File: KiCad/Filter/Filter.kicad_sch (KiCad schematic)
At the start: 31 parts, among them J1 Screw_Terminal_01x03, J2 Screw_Terminal_01x03, U1 TL074, U2 TL074

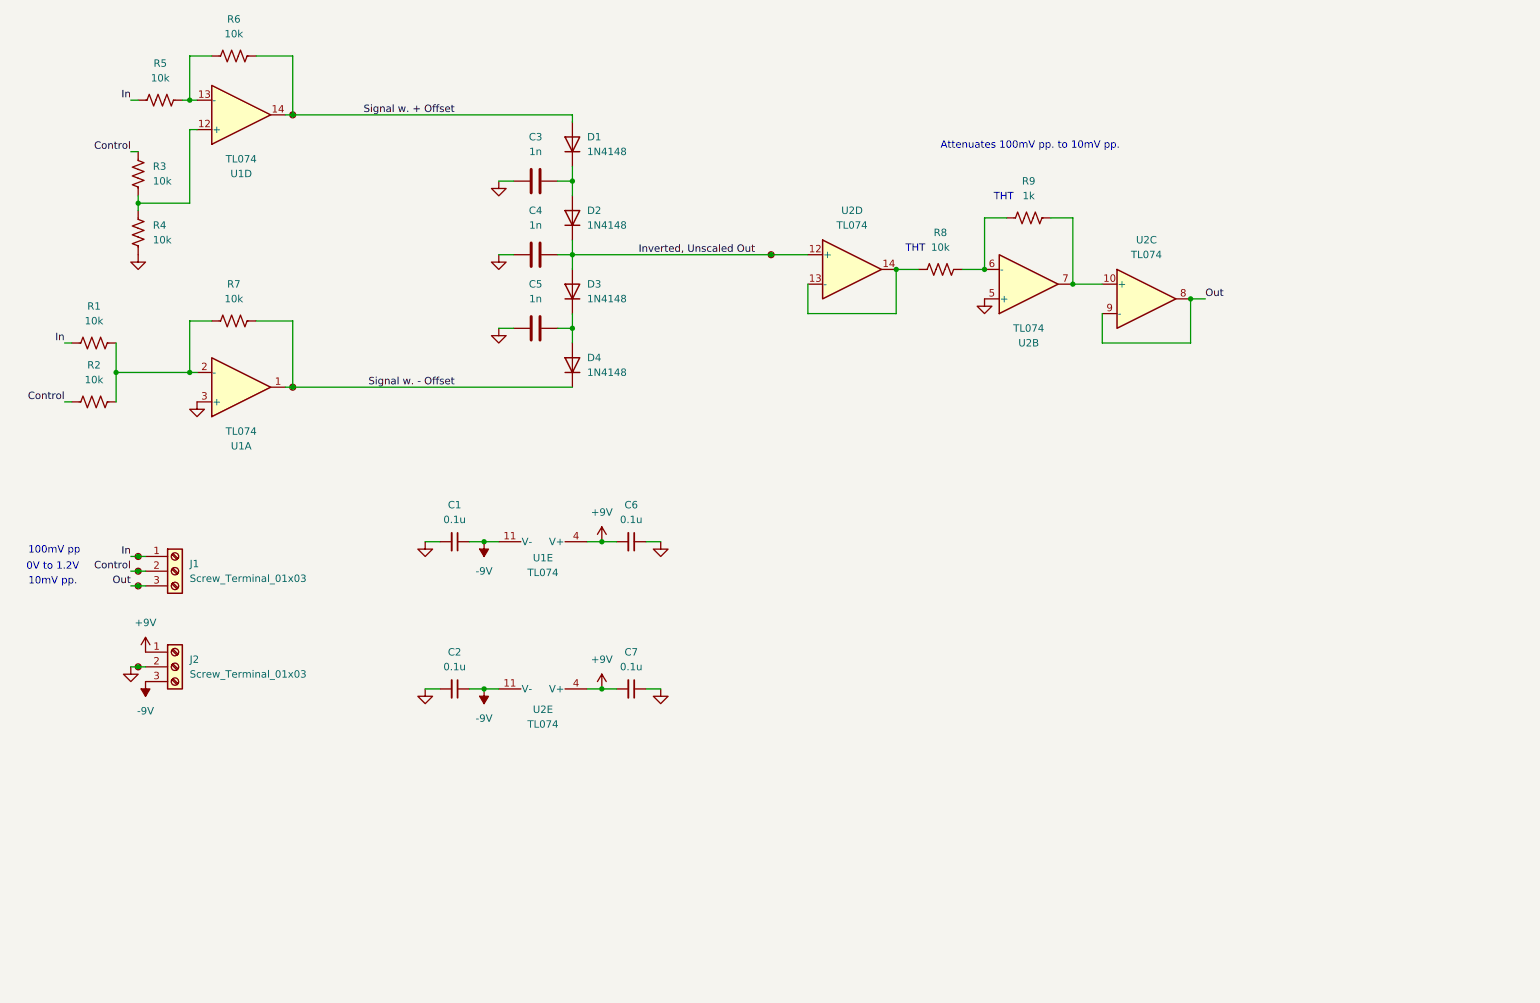
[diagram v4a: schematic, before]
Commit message: added power indicator LEDs
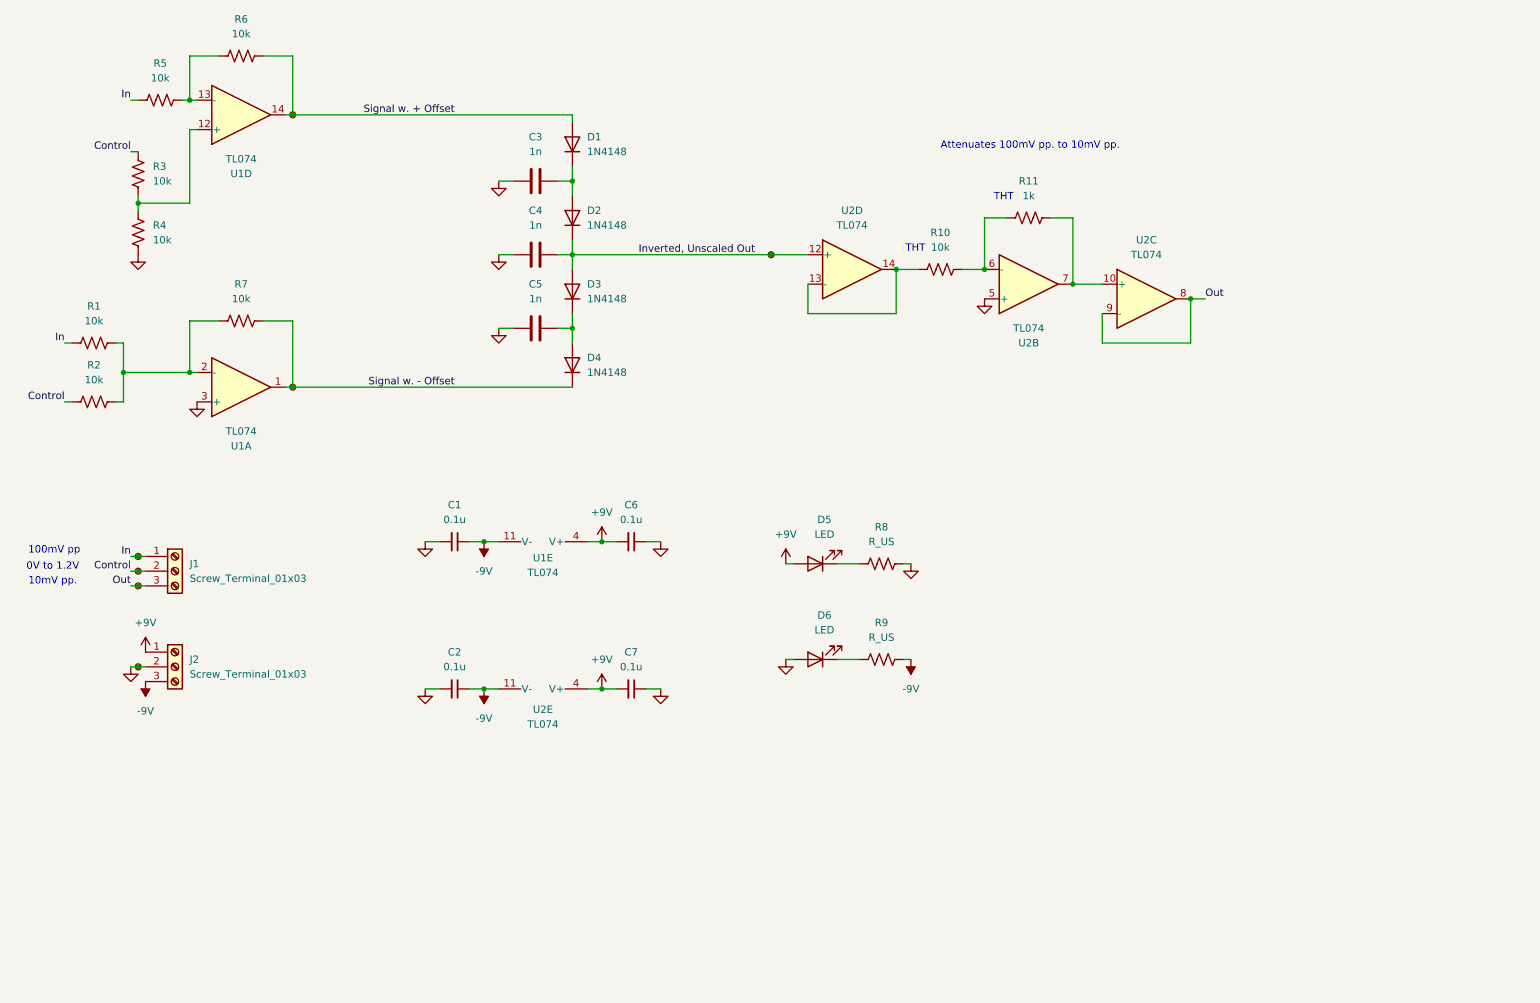
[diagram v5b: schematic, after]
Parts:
- added D5, D6: LED, symbol Device:LED
- added R8, R9: R_US, symbol Device:R_US
- gave numbers to parts that had none: 7
- renumbered R8 to R10, R9 to R11
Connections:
- net +9V: now also D5.2 (A)
- net -9V: now also R9.2
- net GND: now also D6.2 (A), R8.2
- new net: D5.1 (K), R8.1
- new net: D6.1 (K), R9.1
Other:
- moved on the sheet: R6, R7

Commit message: removed unnecessary buffer before filter's output
this drops the number of op amps from 5 to 4, allowing us to use 1 IC instead of 2 ICs with 3 unused circuits.
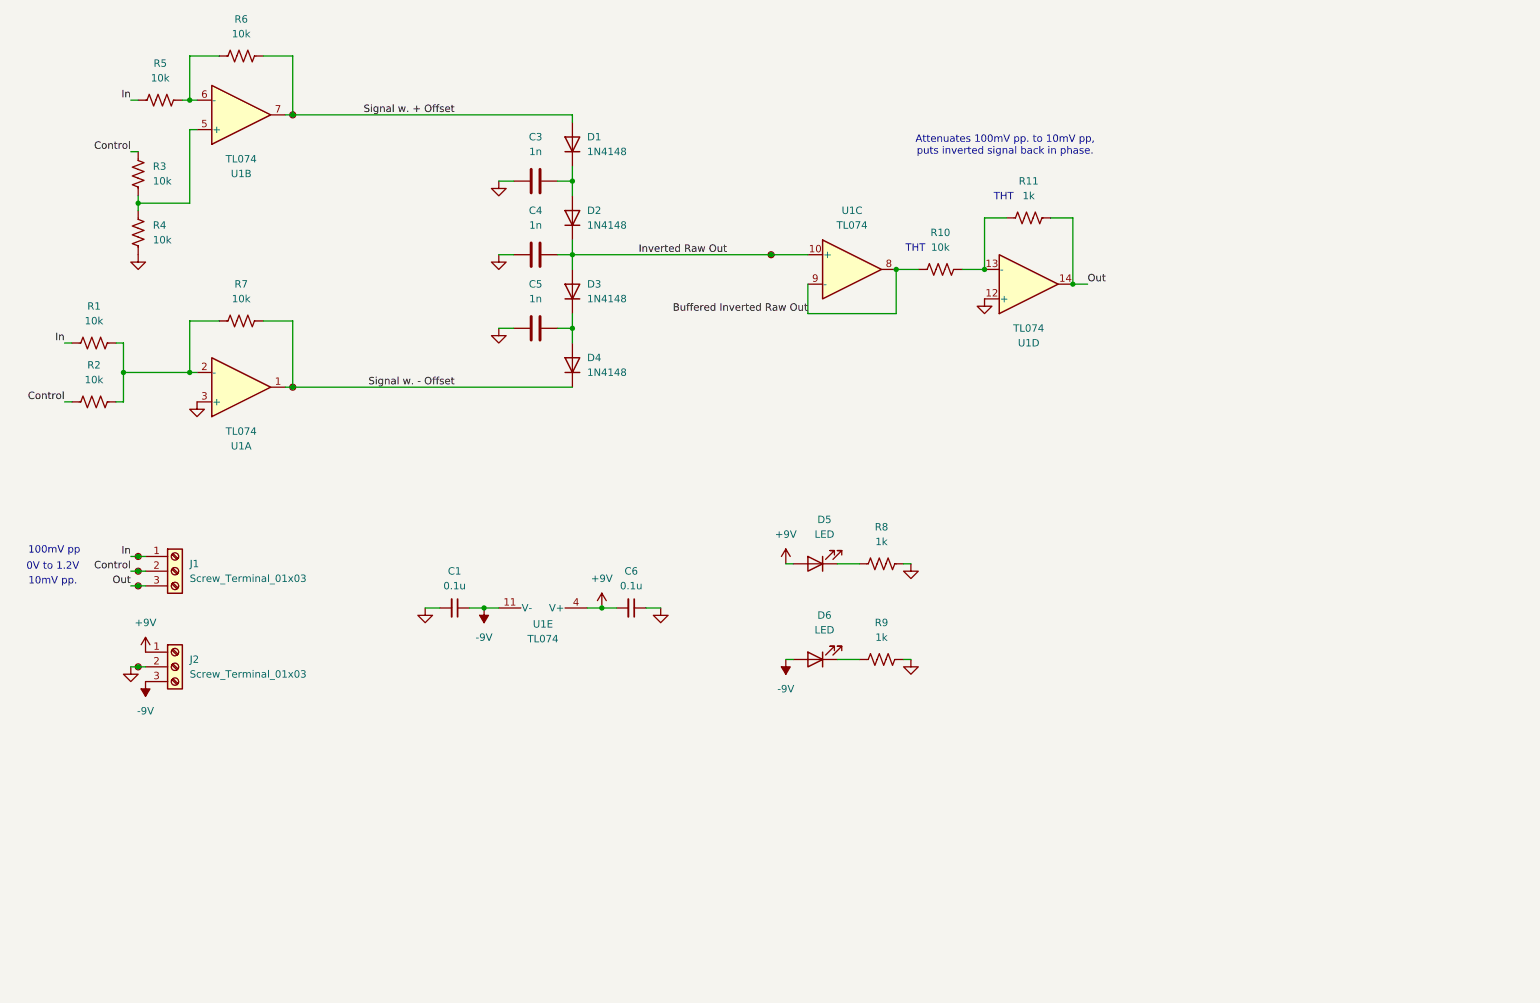
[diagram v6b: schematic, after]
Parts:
- removed C2, C7: 0.1u, symbol Device:C_Small
- removed unit 3 of U2
- removed unit 5 of U2
- C1, C6: footprint (none) -> Capacitor_SMD:C_0805_2012Metric
- D5, D6: footprint (none) -> LED_THT:LED_D5.0mm
- J1, J2: footprint (none) -> Header 691137710003:691137710003
- R1, R2, R3, R4, R5, R6, R7: footprint Resistor_SMD:R_0603_1608Metric -> Resistor_SMD:R_0805_2012Metric
- R8, R9: value R_US -> 1k; footprint (none) -> Resistor_SMD:R_0805_2012Metric
- TP1, TP2, TP3, TP4, TP5, TP6, TP7: footprint (none) -> TestPoint:TestPoint_Keystone_5000-5004_Miniature
- renumbered U2 to U1
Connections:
- net -9V: now also D6.2 (A); no longer R9.2
- net GND: now also R9.2, U1.12 (+); no longer D6.2 (A), U1.5 (+)
- net Out: now also R11.2, U1.14
- net Signal w. + Offset: now also U1.7; no longer U1.14
- net at R10.2, R11.1: now also U1.13 (-); no longer U1.6 (-)
- net at R5.2, R6.1: now also U1.6 (-); no longer U1.13 (-)
- net at R3.1, R4.2: now also U1.5 (+); no longer U1.12 (+)
- net Inverted, Unscaled Out renamed Inverted Raw Out
- net Inverted Raw Out: now also U1.10 (+); no longer U1.12 (+)
- new net Buffered Inverted Raw Out: R10.1, U1.8, U1.9 (-)
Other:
- note added: "Attenuates 100mV pp. to 10mV pp, puts inverted signal back in phase."
- note removed: "Attenuates 100mV pp. to 10mV pp."
- moved on the sheet: C1, C6, U1E

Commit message: added mounting holes to schematics, adjusted board sizes
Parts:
- added H1, H2, H3, H4: MountingHole, MountingHole:MountingHole_3.2mm_M3, symbol Mechanical:MountingHole

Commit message: added protection resistor to diode ladder
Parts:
- added R12: 2.2k, Resistor_SMD:R_0805_2012Metric, symbol Device:R_US
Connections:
- net Signal w. + Offset: now also R12.1; no longer D1.2 (A)
- new net: D1.2 (A), R12.2
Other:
- note added: "Protective resistor. When the voltage across the diode ladder becomes too high, then the diodes short, which may destroy the op amps."
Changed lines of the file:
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@@
 		)
 	)
+	(text "Protective resistor.\nWhen the voltage across the diode ladder\nbecomes too high, then the diodes short,\nwhich may destroy the op amps."
+		(exclude_from_sim no)
+		(at 108.458 26.67 0)
+		(effects
+			(font
+				(size 1.27 1.27)
+			)
+		)
+	)
 	(text "Attenuates 100mV pp. to 10mV pp,\nputs inverted signal back in phase."
 		(exclude_from_sim no)
@@
 	(wire
 		(pts
-			(xy 66.04 39.37) (xy 114.3 39.37)
+			(xy 111.76 39.37) (xy 114.3 39.37)
 		)
 		(stroke
@@
 	(wire
 		(pts
+			(xy 66.04 39.37) (xy 104.14 39.37)
+		)
+		(stroke
+			(width 0)
+			(type default)
+		)
+	)
+	(wire
+		(pts
 			(xy 114.3 63.5) (xy 148.59 63.5)
 		)
@@
 				)
 			)
+		)
+	)
+	(symbol
+		(lib_id "Device:R_US")
+		(at 107.95 39.37 90)
+		(unit 1)
+		(body_style 1)
+		(exclude_from_sim no)
+		(in_bom yes)
+		(on_board yes)
+		(in_pos_files yes)
+		(dnp no)
+		(fields_autoplaced yes)
+		(property "Reference" "R12"
+			(at 107.95 33.02 90)
+			(show_name no)
+			(do_not_autoplace no)
+			(effects
+				(font
+					(size 1.27 1.27)
+				)
+			)
+		)
+		(property "Value" "2.2k"
+			(at 107.95 35.56 90)
+			(show_name no)
+			(do_not_autoplace no)
+			(effects
+				(font
+					(size 1.27 1.27)
+				)
+			)
+		)
+		(property "Footprint" "Resistor_SMD:R_0805_2012Metric"
+			(at 108.204 38.354 90)
+			(hide yes)
+			(show_name no)
+			(do_not_autoplace no)
+			(effects
+				(font
+					(size 1.27 1.27)
+				)
+			)
+		)
+		(property "Datasheet" ""
+			(at 107.95 39.37 0)
+			(hide yes)
+			(show_name no)
+			(do_not_autoplace no)
+			(effects
+				(font
+					(size 1.27 1.27)
+				)
+			)
+		)
+		(property "Description" "Resistor, US symbol"
+			(at 107.95 39.37 0)
+			(hide yes)
+			(show_name no)
+			(do_not_autoplace no)
+			(effects
+				(font
+					(size 1.27 1.27)
+				)
+			)
+		)
+		(property "LCSC Part #" ""
+			(at 107.95 39.37 90)
+			(hide yes)
+			(show_name no)
+			(do_not_autoplace no)
+			(effects
+				(font
+					(size 1.27 1.27)
+				)
+			)
+		)
+		(pin "1"
+		)
+		(pin "2"
+		)
+		(instances
+			(project "Filter"
+				(path "/d0463ce5-c32c-4d9a-94ac-2a0e117a03ce"
+					(reference "R12")
+					(unit 1)
+				)
+			)
